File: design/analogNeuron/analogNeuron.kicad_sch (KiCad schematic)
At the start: 104 parts, among them J1 Conn_01x02_Pin, J2 Conn_02x20_Counter_Clockwise, J3 Conn_01x02_Pin, J4 Conn_02x06_Counter_Clockwise, J5 Conn_02x06_Counter_Clockwise, J6 Conn_01x02_Pin, J7 Conn_01x02_Pin, Q1 2N3904, Q2 2N3904, U2 LM13700

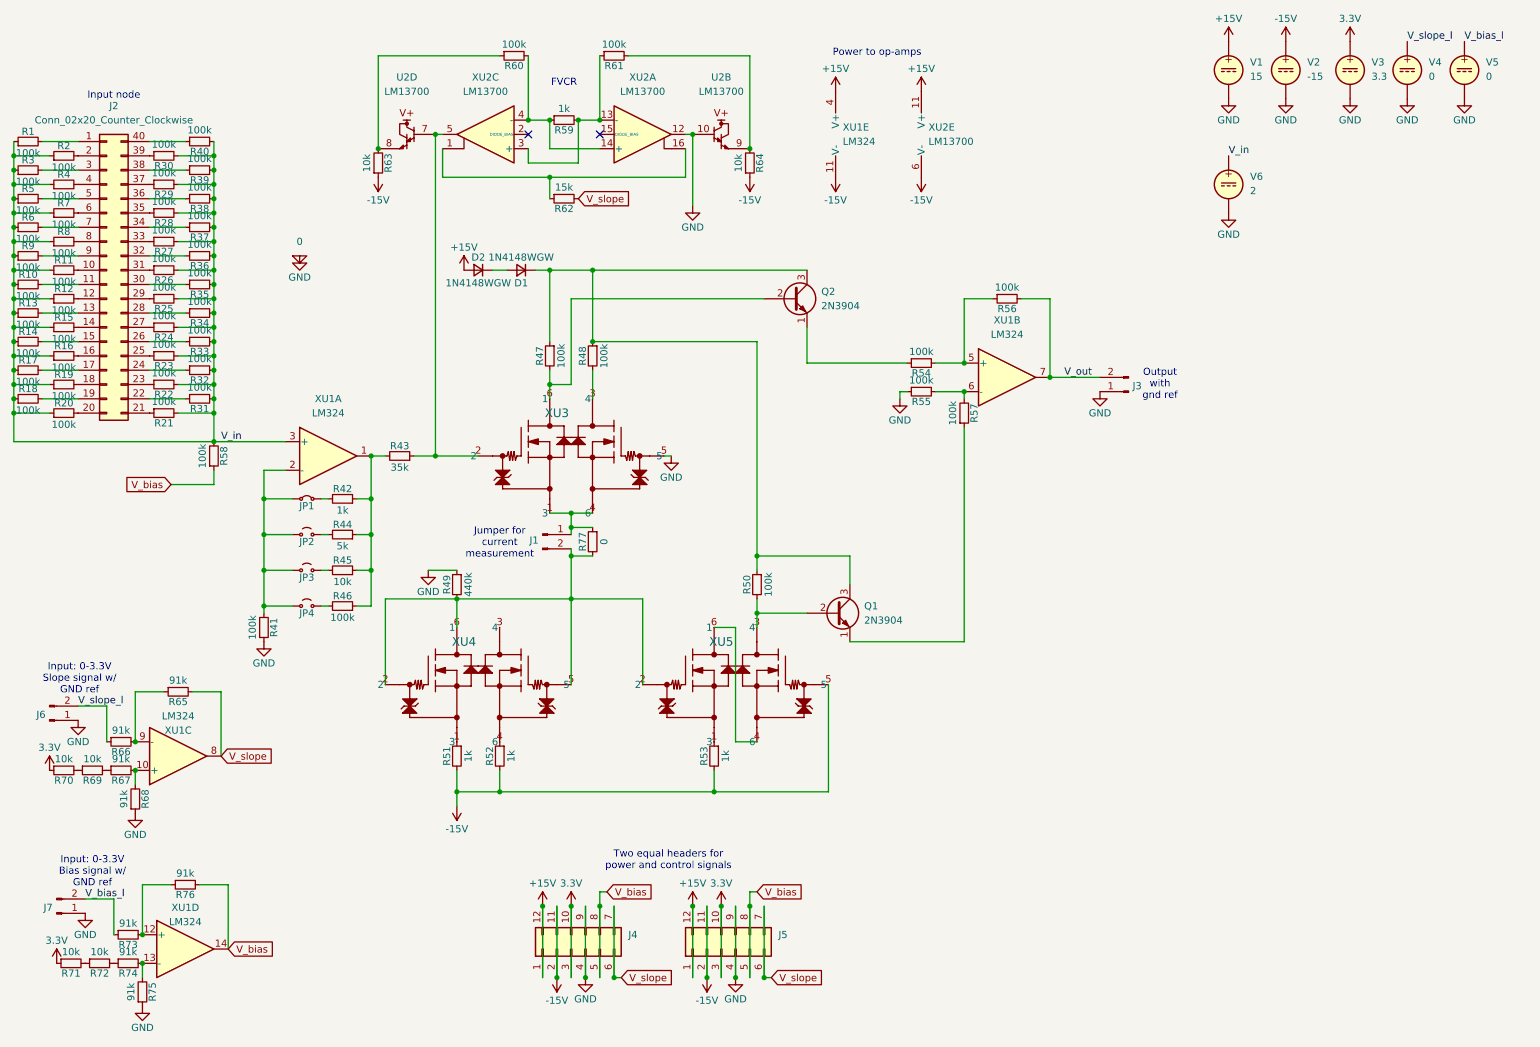
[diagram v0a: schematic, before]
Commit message: Activation function now simulated
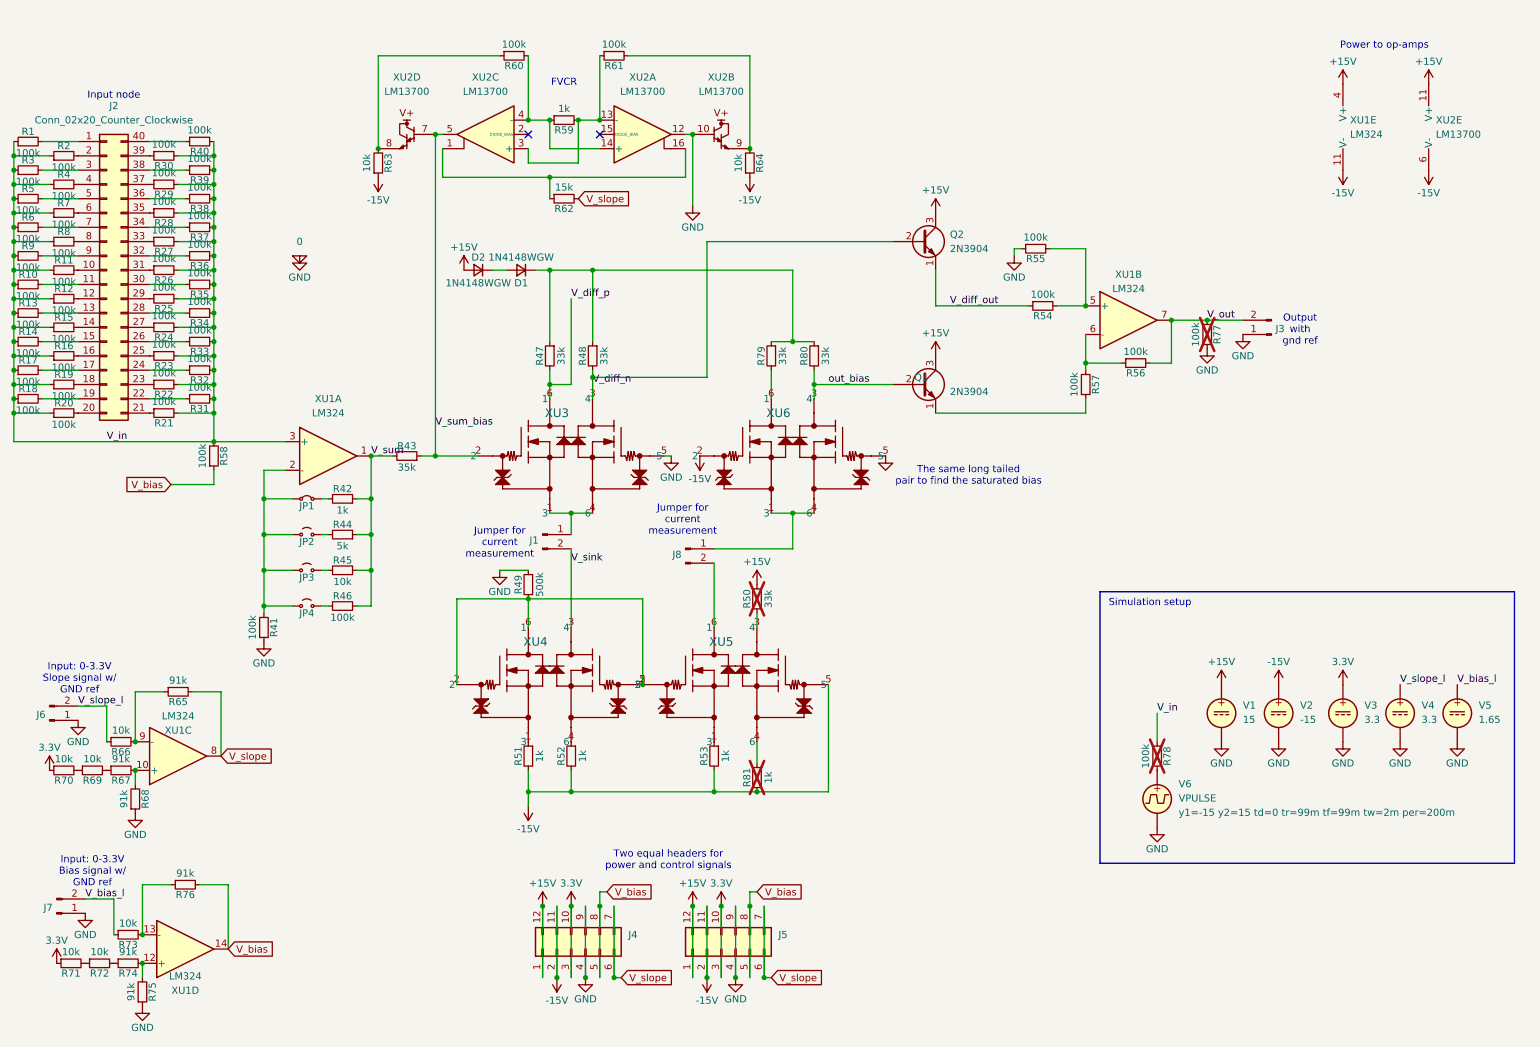
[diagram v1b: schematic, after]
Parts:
- removed V6: 2, symbol Simulation_SPICE:VDC
- added J8: Conn_01x02_Pin, Connector_PinHeader_2.54mm:PinHeader_1x02_P2.54mm_Vertical, symbol Connector:Conn_01x02_Pin
- added R78: 100k, symbol Device:R_Small
- added R79, R80: 33k, Resistor_SMD:R_0402_1005Metric, symbol Device:R_Small
- added R81: 1k, symbol Device:R_Small
- added V6: VPULSE, symbol Simulation_SPICE:VPULSE
- added XU6: SSM6N7002CFU_LF, SOT-363 US6_TOS, symbol ul_SSM6N7002CFU-LF:SSM6N7002CFU_LF
- R47, R48: value 100k -> 33k
- R49: value 440k -> 500k
- R50: value 100k -> 33k; footprint Resistor_SMD:R_0402_1005Metric -> (none); now not fitted
- R66, R73: value 91k -> 10k
- R77: value 0 -> 100k; footprint Resistor_SMD:R_0402_1005Metric -> (none); now not fitted
- V4: value 0 -> 3.3
- V5: value 0 -> 1.65
- renumbered U2 to XU2
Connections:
- net +15V: now also Q1.3 (C), Q2.3 (C), R50.1
- net -15V: now also R81.2, XU6.2
- net 0: now also R77.1, V6.2, XU6.5
- net V_in: now also R78.2
- net V_out: now also R77.2
- net at D1.1 (K), R47.1, R48.1: now also R79.1, R80.1; no longer Q1.3 (C), Q2.3 (C), R50.1
- net V_diff_p: now reaches R47.2, XU3.6 (1)
- net V_diff_p: no longer Q2.2 (B)
- net V_diff_out: now reaches Q2.1 (E), R54.1
- net at J1.1 (Pin_1), XU3.1 (3), XU3.4 (6): no longer R77.1
- net at R49.2, XU4.2, XU4.5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: no longer J1.2 (Pin_2), R77.2
- net V_diff_n: now reaches R48.2, XU3.3 (4)
- net V_diff_n: now also Q2.2 (B)
- net at R50.2, XU5.3 (4): no longer Q1.2 (B)
- net V_sum_bias: now reaches R43.1, XU2.5, XU2.7, XU3.2
- net V_sink: now reaches XU4.3 (4)
- net V_sink: now also J1.2 (Pin_2)
- net at R54.2, XU1.5 (+): now also R55.2; no longer R56.1
- net at R57.2, XU1.6 (-): now also R56.1; no longer R55.2
- net at R73.2, R76.1: now also XU1.13 (-); no longer XU1.12 (+)
- net at R74.2, R75.2: now also XU1.12 (+); no longer XU1.13 (-)
- net V_sum: now reaches R42.1, R43.2, R44.1, R45.1, R46.1, XU1.1
- net at XU5.4 (6): now also R81.1; no longer XU5.6 (1)
- new net: J8.1 (Pin_1), XU6.1 (3), XU6.4 (6)
- new net: R79.2, XU6.6 (1)
- new net: J8.2 (Pin_2), XU5.6 (1)
- new net: R78.1, V6.1
- new net out_bias: Q1.2 (B), R80.2, XU6.3 (4)
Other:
- note added: "Simulation setup"
- note added: "The same long tailed pair to find the saturated bias"
- moved on the sheet: J3, Q2, R43, R49, R51, R52, R54, R57, V1, V2, V3, V4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
